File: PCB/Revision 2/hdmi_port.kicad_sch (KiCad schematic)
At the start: 1 part, among them J7 HDMI_A

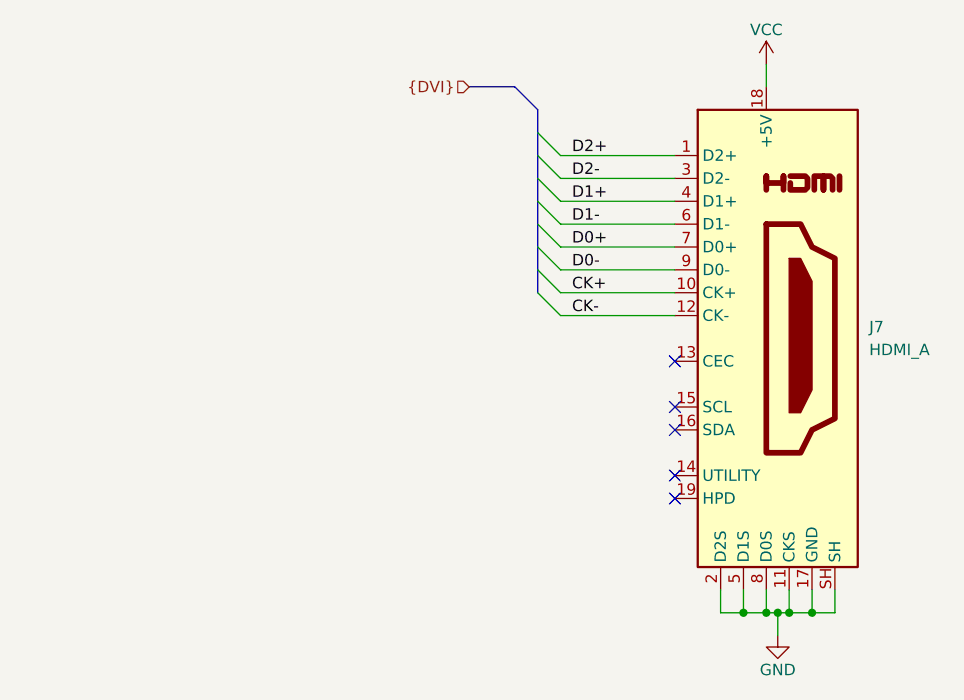
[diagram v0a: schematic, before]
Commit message: ESD protection diodes go BRRRRRRR
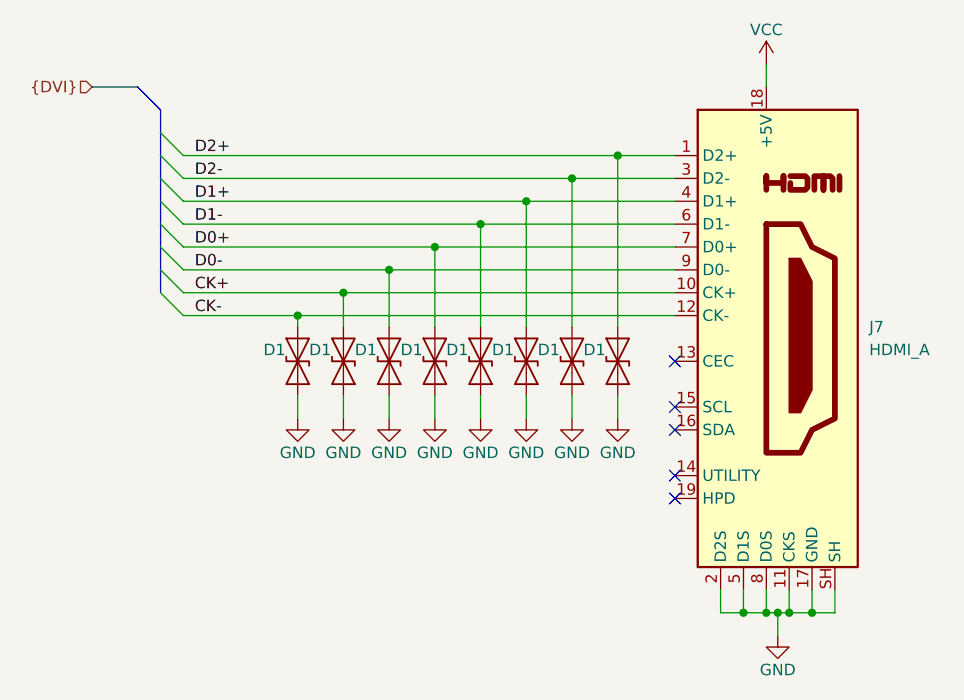
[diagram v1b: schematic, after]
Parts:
- added D1 (x8): ESD9B3.3ST5G, Diode_SMD:D_SOD-923, symbol Diode:ESD9B3.3ST5G
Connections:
- net CK+: now also D1.1 (A1)
- net CK-: now also D1.1 (A1)
- net D0+: now also D1.1 (A1)
- net D0-: now also D1.1 (A1)
- net D1+: now also D1.1 (A1)
- net D1-: now also D1.1 (A1)
- net D2+: now also D1.1 (A1)
- net D2-: now also D1.1 (A1)
- net GND: now also D1.2 (A2), D1.2 (A2), D1.2 (A2), D1.2 (A2), D1.2 (A2), D1.2 (A2), D1.2 (A2), D1.2 (A2)
